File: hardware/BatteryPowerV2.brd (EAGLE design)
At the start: 47 x 40.5 mm, 66 parts, among them Q1 IRLML6402, U1 LT1616ES6TRMPBF, U2 LT6106CS5#PBF, U3 LT1616ES6TRMPBF, U4 LT6106CS5#PBF, U5 TCK106AF,LF, U6 TCK106AF,LF

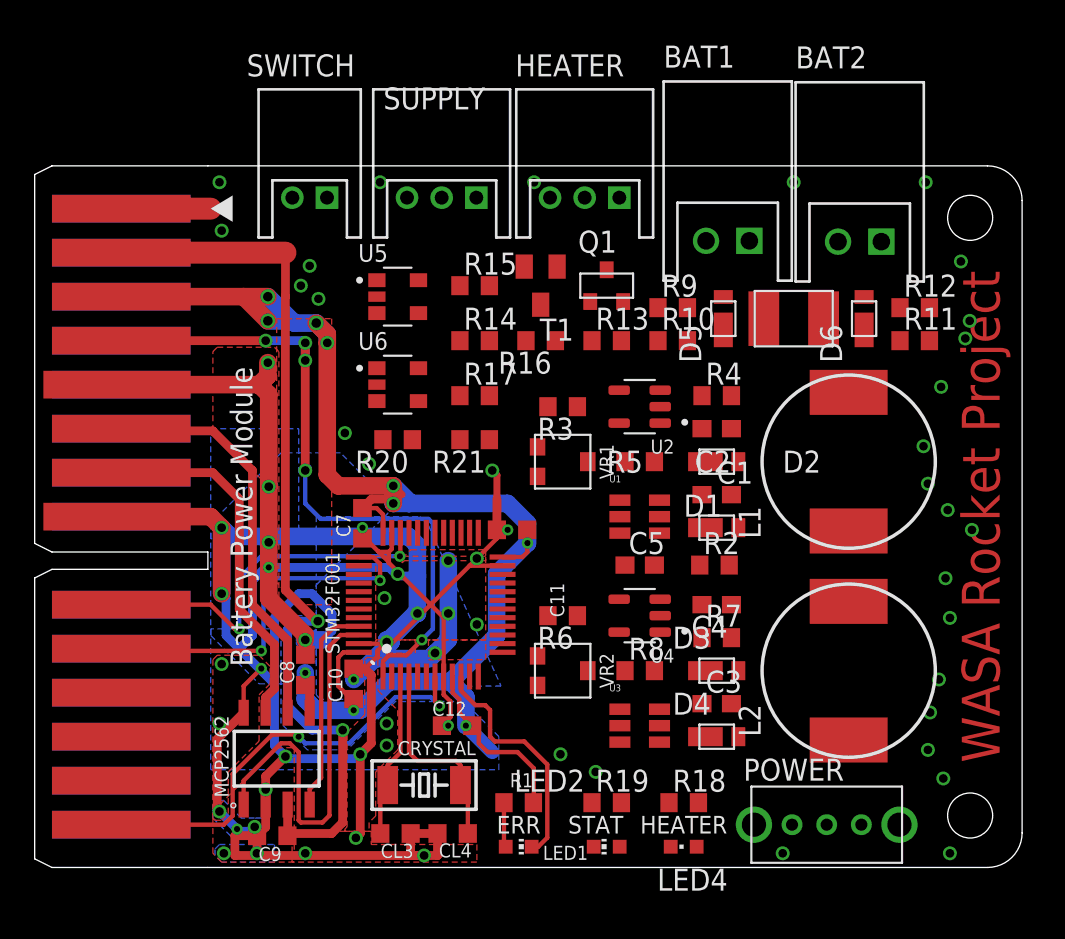
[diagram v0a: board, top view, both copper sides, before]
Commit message: BatteryPowerV2とINSの基板設計です。変えたつもりはないんですけど、schの方が変わっちゃってる可能性があって、申し訳ないんですけど確認お願いします。
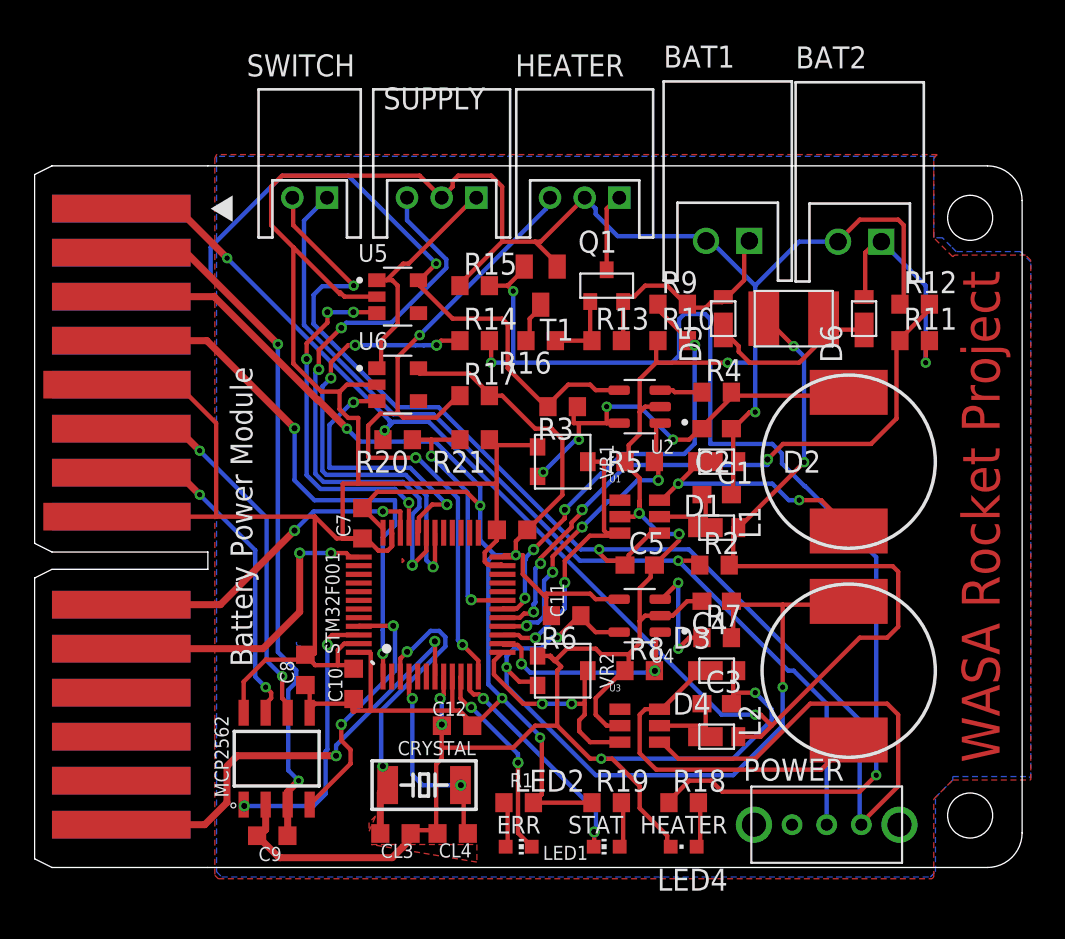
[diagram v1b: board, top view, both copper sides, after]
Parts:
- moved R12 0.20 mm to (50.8, 12.3)
- moved R9 0.20 mm to (36.8, 12.3)
- moved C4 0.20 mm to (39.4, -4.88)
- moved R4 0.20 mm to (39.4, 7.18)
- moved R6 0.20 mm to (30.7, -5.71)
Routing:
- net GND: track 196.4 -> 289.5 mm, vias 65 -> 8
- net VPP: track 5.16 -> 93.8 mm, vias 0 -> 5
- net !SHDN!: track 0.00 -> 86.0 mm, vias 0 -> 2
- net N$10: track 0.00 -> 69.4 mm, vias 0 -> 3
- net N$7: track 0.00 -> 55.5 mm, vias 0 -> 1
- net 3V3: track 0.00 -> 47.4 mm, vias 0 -> 3
- net TEMP: track 0.00 -> 41.2 mm, vias 0 -> 3
- net BAT2_V: track 0.00 -> 37.4 mm, vias 0 -> 4
- net SUPPLY_CON: track 0.00 -> 34.4 mm, vias 0 -> 3
- net VCC: track 52.3 -> 83.2 mm, vias 2 -> 3
- net HEATER: track 0.00 -> 27.5 mm, vias 0 -> 4
- net BAT1_V: track 0.00 -> 26.1 mm, vias 0 -> 4
- net 5V: track 0.00 -> 25.7 mm, vias 0 -> 4
- net SUPPLY_5V: track 0.00 -> 21.1 mm, vias 0 -> 4
- net VDD_SW: track 0.00 -> 20.3 mm
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
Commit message: 大変お待たせしました。BatteryPowerV2とINSの改良版です。確認お願いします。
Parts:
- moved C7 1.70 mm to (17.2, -0.48)
- moved C12 0.30 mm to (24.4, -12.4)
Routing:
- net !SHDN!: track 86.0 -> 73.3 mm, vias 2 -> 3
- net GND: track 289.5 -> 278.6 mm, vias 8 -> 27
- net VCC: track 83.2 -> 91.0 mm
- net 3V3: track 47.4 -> 52.6 mm
- net SUPPLY_CON: track 34.4 -> 38.4 mm
- net SUPPLY_5V: track 21.1 -> 24.9 mm, vias 4 -> 2
- net VDD: track 110.5 -> 114.3 mm
- net N$6: track 6.88 -> 4.39 mm
- net CAN_TX: track 15.9 -> 13.6 mm
- net BAT1: track 13.8 -> 16.0 mm
- net BAT1_V: track 26.1 -> 28.0 mm
- net N$7: track 55.5 -> 53.5 mm
- net HEATER: track 27.5 -> 29.3 mm
- net SWCLK1: track 18.1 -> 16.7 mm
- net VBAT: track 31.9 -> 30.5 mm
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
